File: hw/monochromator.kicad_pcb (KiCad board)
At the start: 2 copper layers, 120 x 45 mm, 45 parts, among them J1 USB_B, J2 UART_01X03, J3 IDC_02X03, J4 SWD_01X04, J5 Power_Terminal, J6 Screw_Terminal, SW1 SW_Push, U1 USBLC6-2SC6, U2 STM32F072CBTx, U3 CP2102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

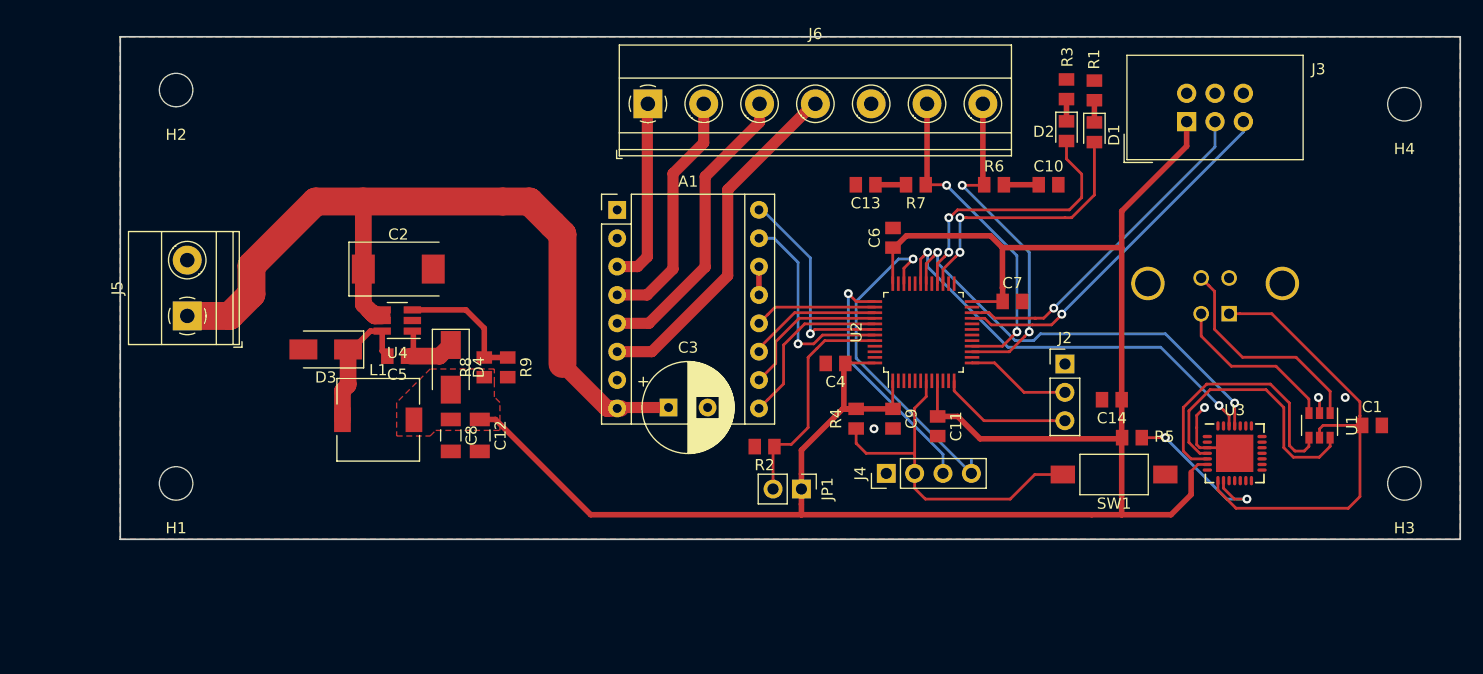
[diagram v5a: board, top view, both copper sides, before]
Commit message: updated footprint placement and updated layout CP1202
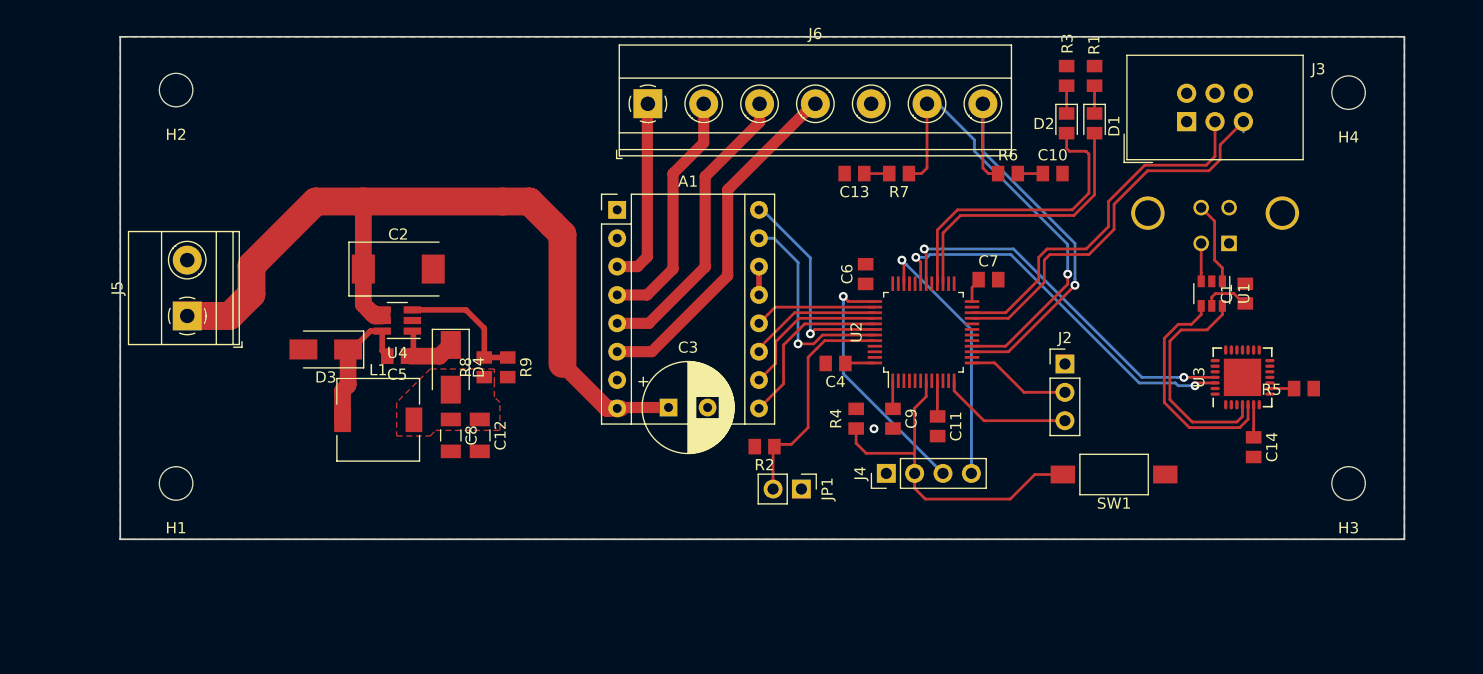
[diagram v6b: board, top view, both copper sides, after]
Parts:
- moved C1 16.4 mm to (185.8, 83.0), turned to 90 degrees
- moved R5 16.0 mm to (191.0, 91.5), turned to 180 degrees
- moved U1 15.2 mm to (182.8, 83.0)
- moved C14 13.4 mm to (186.5, 96.8), turned to 270 degrees
- moved U3 6.84 mm to (185.5, 90.5), turned to 90 degrees
- moved J1 6.30 mm to (184.3, 78.5)
- moved H4 5.11 mm to (195.0, 65.0)
- moved H3 5.00 mm to (195.0, 100.0)
- moved C6 4.07 mm to (151.8, 81.2)
- moved C7 2.90 mm to (162.8, 81.8)
- moved R7 1.80 mm to (154.8, 72.2)
- moved R6 1.60 mm to (164.5, 72.2)
- moved C13 1.41 mm to (150.8, 72.2)
- moved R1 1.30 mm to (172.2, 63.5)
- moved R3 1.20 mm to (169.8, 63.5)
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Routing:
- net +3V3: track 188.2 -> 13.0 mm
- net Net-(C1-Pad1): track 42.7 -> 4.28 mm
- net Net-(R5-Pad2): track 14.9 -> 2.17 mm, vias 2 -> 0
- net Net-(J1-Pad3): track 19.7 -> 7.39 mm
- net Net-(J1-Pad2): track 15.2 -> 3.61 mm
- net /END_STOP2: track 29.9 -> 40.4 mm, vias 2 -> 1
- net GND: track 8.96 -> 0.00 mm, vias 4 -> 1
- net /END_STOP1: track 31.1 -> 38.7 mm, vias 2 -> 1
- net /SWD_IO: track 30.1 -> 25.1 mm
- net /UART_USB_TX: track 38.5 -> 34.0 mm
- net Net-(U1-Pad6): track 24.1 -> 20.3 mm
- net /UART_USB_RX: track 37.8 -> 34.4 mm
- net Net-(U1-Pad4): track 24.1 -> 20.8 mm
- net /UART_PANEL_RX: track 32.7 -> 35.8 mm, vias 1 -> 0
- net /UART_PANEL_TX: track 30.7 -> 33.2 mm, vias 1 -> 0
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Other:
- board size 120 x 45 mm -> 115 x 45 mm

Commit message: updated layout and reduced pcb size
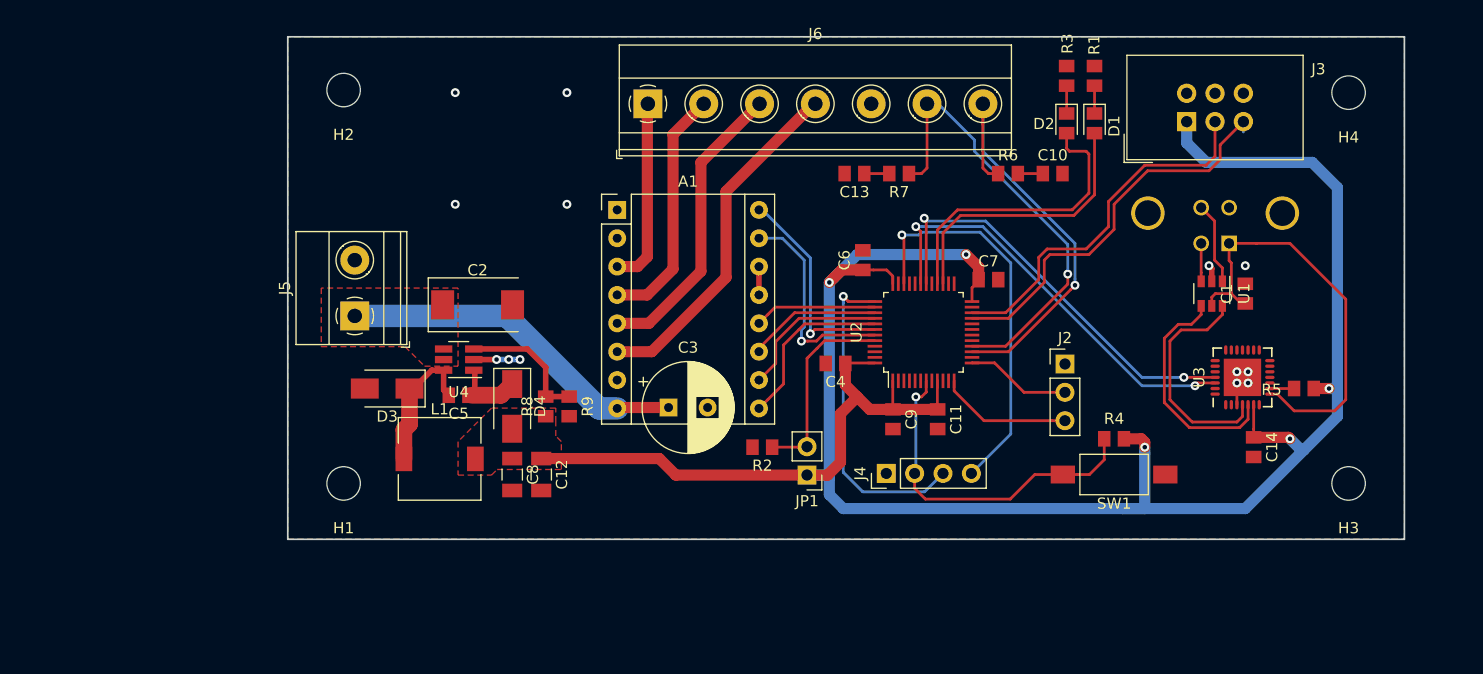
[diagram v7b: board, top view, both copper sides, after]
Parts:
- moved R4 23.2 mm to (174.0, 96.0), turned to 180 degrees
- moved H1 15.0 mm to (105.0, 100.0)
- moved H2 15.0 mm to (105.0, 64.8)
- moved J5 15.0 mm to (106.0, 85.0)
- moved C2 7.79 mm to (117.0, 84.0)
- moved C12 6.52 mm to (122.7, 99.2)
- moved C5 6.52 mm to (115.3, 92.1)
- moved C8 6.52 mm to (120.1, 99.2)
- moved D3 6.52 mm to (108.9, 91.5)
- moved D4 6.52 mm to (120.1, 93.1)
- moved L1 6.52 mm to (113.6, 97.8)
- moved R8 6.52 mm to (123.1, 93.1)
- moved R9 6.52 mm to (125.2, 93.1)
- moved U4 6.52 mm to (115.3, 88.9)
- moved JP1 1.35 mm to (146.5, 99.2), turned to 180 degrees
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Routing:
- net +3V3: track 13.0 -> 206.2 mm, vias 0 -> 5
- net +12V: track 78.0 -> 31.6 mm
- net Net-(C1-Pad1): track 4.28 -> 38.2 mm
- net /SWD_IO: track 25.1 -> 35.7 mm
- net GND: track 0.00 -> 7.60 mm, vias 1 -> 13
- net /SWD_CLK: track 22.6 -> 29.1 mm
- net /UART_USB_TX: track 34.0 -> 37.9 mm
- net /UART_USB_RX: track 34.4 -> 38.1 mm
- net Net-(JP1-Pad2): track 20.7 -> 18.1 mm
- net /~RST: track 31.7 -> 31.2 mm, vias 0 -> 1
- added copper zone on F.Cu, net +12V
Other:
- board size 115 x 45 mm -> 100 x 45 mm

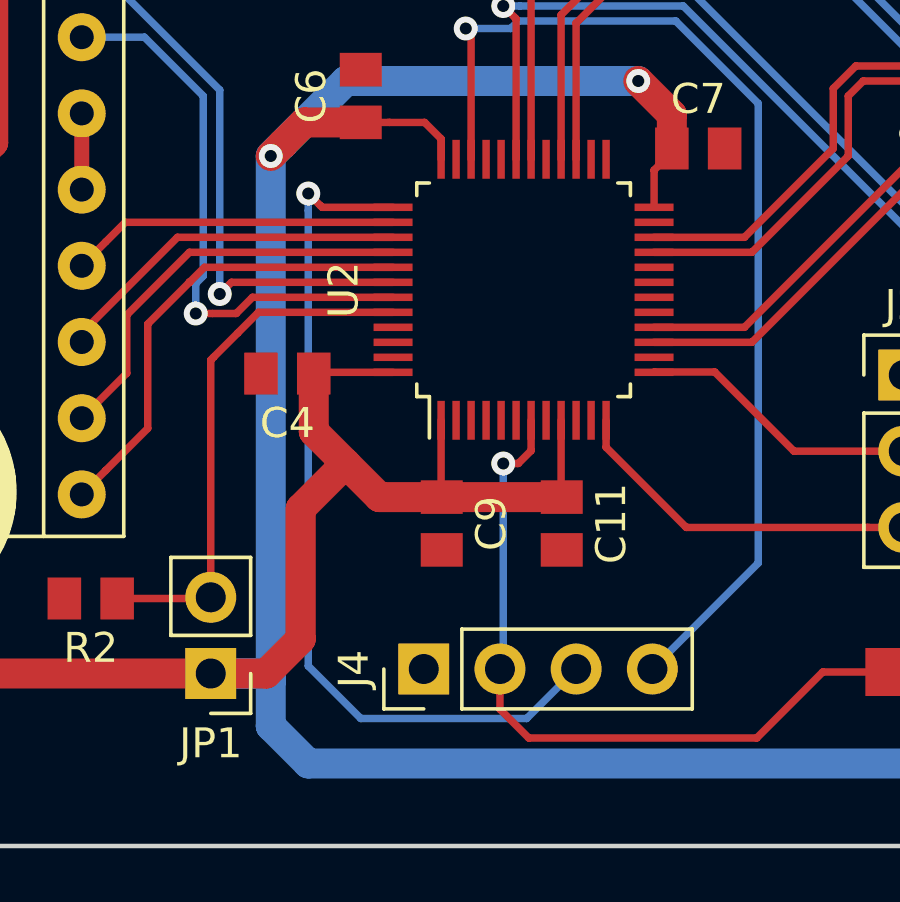
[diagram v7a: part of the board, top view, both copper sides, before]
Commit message: updated SWD_CLK and via under STM32
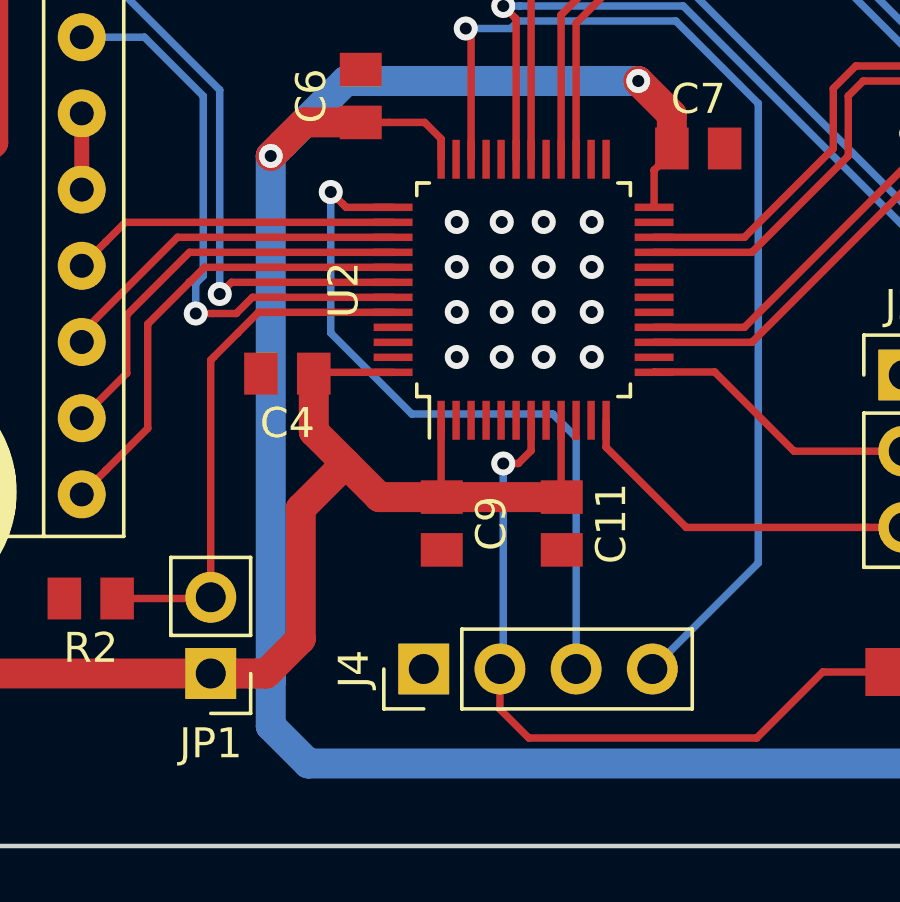
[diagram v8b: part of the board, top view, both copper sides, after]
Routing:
- net /SWD_CLK: track 29.1 -> 24.3 mm
- net GND: vias 13 -> 29
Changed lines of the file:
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@@
     (thickness 1.6)
     (drawings 4)
-    (tracks 346)
+    (tracks 362)
     (zones 0)
     (modules 45)
@@
   )
   (setup
-    (last_trace_width 0.5)
+    (last_trace_width 0.25)
     (user_trace_width 0.5)
     (user_trace_width 0.8)
@@
   (segment (start 127.88 93.28) (end 119.6 85) (width 2) (layer B.Cu) (net 1))
   (segment (start 119.6 85) (end 106 85) (width 2) (layer B.Cu) (net 1))
+  (via (at 156.2 87.2) (size 0.8) (drill 0.4) (layers F.Cu B.Cu) (net 2))
+  (via (at 156.2 85.7) (size 0.8) (drill 0.4) (layers F.Cu B.Cu) (net 2))
+  (via (at 157.6 85.7) (size 0.8) (drill 0.4) (layers F.Cu B.Cu) (net 2))
+  (via (at 157.6 87.2) (size 0.8) (drill 0.4) (layers F.Cu B.Cu) (net 2))
+  (via (at 159.2 87.2) (size 0.8) (drill 0.4) (layers F.Cu B.Cu) (net 2))
+  (via (at 159.2 85.7) (size 0.8) (drill 0.4) (layers F.Cu B.Cu) (net 2))
+  (via (at 157.6 84.2) (size 0.8) (drill 0.4) (layers F.Cu B.Cu) (net 2))
+  (via (at 156.2 84.2) (size 0.8) (drill 0.4) (layers F.Cu B.Cu) (net 2))
+  (via (at 154.7 85.7) (size 0.8) (drill 0.4) (layers F.Cu B.Cu) (net 2))
+  (via (at 154.7 87.2) (size 0.8) (drill 0.4) (layers F.Cu B.Cu) (net 2))
+  (via (at 157.6 88.7) (size 0.8) (drill 0.4) (layers F.Cu B.Cu) (net 2))
+  (via (at 156.2 88.7) (size 0.8) (drill 0.4) (layers F.Cu B.Cu) (net 2))
+  (via (at 154.7 88.7) (size 0.8) (drill 0.4) (layers F.Cu B.Cu) (net 2))
+  (via (at 159.2 88.7) (size 0.8) (drill 0.4) (layers F.Cu B.Cu) (net 2))
+  (via (at 159.2 84.2) (size 0.8) (drill 0.4) (layers F.Cu B.Cu) (net 2))
+  (via (at 154.7 84.2) (size 0.8) (drill 0.4) (layers F.Cu B.Cu) (net 2))
   (segment (start 119.8 88.9) (end 120.8 88.9) (width 0.5) (layer B.Cu) (net 2))
   (via (at 120.8 88.9) (size 0.8) (drill 0.4) (layers F.Cu B.Cu) (net 2))
@@
   (segment (start 155.178 82.11) (end 155.178 77.928002) (width 0.25) (layer F.Cu) (net 50))
   (via (at 154.999998 77.75) (size 0.8) (drill 0.4) (layers F.Cu B.Cu) (net 50))
-  (segment (start 149.75 99) (end 149.75 83.815717) (width 0.25) (layer B.Cu) (net 51))
-  (segment (start 157.03 100.75) (end 151.5 100.75) (width 0.25) (layer B.Cu) (net 51))
-  (segment (start 151.5 100.75) (end 149.75 99) (width 0.25) (layer B.Cu) (net 51))
-  (segment (start 158.68 99.1) (end 157.03 100.75) (width 0.25) (layer B.Cu) (net 51))
-  (segment (start 149.75 83.815717) (end 149.75 83.250032) (width 0.25) (layer B.Cu) (net 51))
-  (segment (start 150.209968 83.71) (end 150.149999 83.650031) (width 0.25) (layer F.Cu) (net 51))
-  (segment (start 152.578 83.71) (end 150.209968 83.71) (width 0.25) (layer F.Cu) (net 51))
-  (segment (start 150.149999 83.650031) (end 149.75 83.250032) (width 0.25) (layer F.Cu) (net 51))
-  (via (at 149.75 83.250032) (size 0.8) (drill 0.4) (layers F.Cu B.Cu) (net 51))
+  (segment (start 153.2 90.6) (end 150.5 87.9) (width 0.25) (layer B.Cu) (net 51))
+  (segment (start 150.5 87.9) (end 150.5 83.2) (width 0.25) (layer B.Cu) (net 51))
+  (segment (start 158.68 91.38) (end 157.9 90.6) (width 0.25) (layer B.Cu) (net 51))
+  (segment (start 157.9 90.6) (end 153.2 90.6) (width 0.25) (layer B.Cu) (net 51))
+  (segment (start 151.01 83.71) (end 150.899999 83.599999) (width 0.25) (layer F.Cu) (net 51))
+  (segment (start 152.578 83.71) (end 151.01 83.71) (width 0.25) (layer F.Cu) (net 51))
+  (segment (start 158.68 99.1) (end 158.68 91.38) (width 0.25) (layer B.Cu) (net 51))
+  (via (at 150.5 83.2) (size 0.8) (drill 0.4) (layers F.Cu B.Cu) (net 51))
+  (segment (start 150.899999 83.599999) (end 150.5 83.2) (width 0.25) (layer F.Cu) (net 51))
   (segment (start 142.999999 84.860001) (end 142.2 85.66) (width 0.25) (layer F.Cu) (net 52))
   (segment (start 152.578 84.21) (end 143.65 84.21) (width 0.25) (layer F.Cu) (net 52))
